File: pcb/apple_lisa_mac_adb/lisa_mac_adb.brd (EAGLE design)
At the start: 56 x 65 mm, 54 parts, among them IC1 STM32F072C8T6, SW1 324_SW, SW2 324_SW, SW3 324_SW

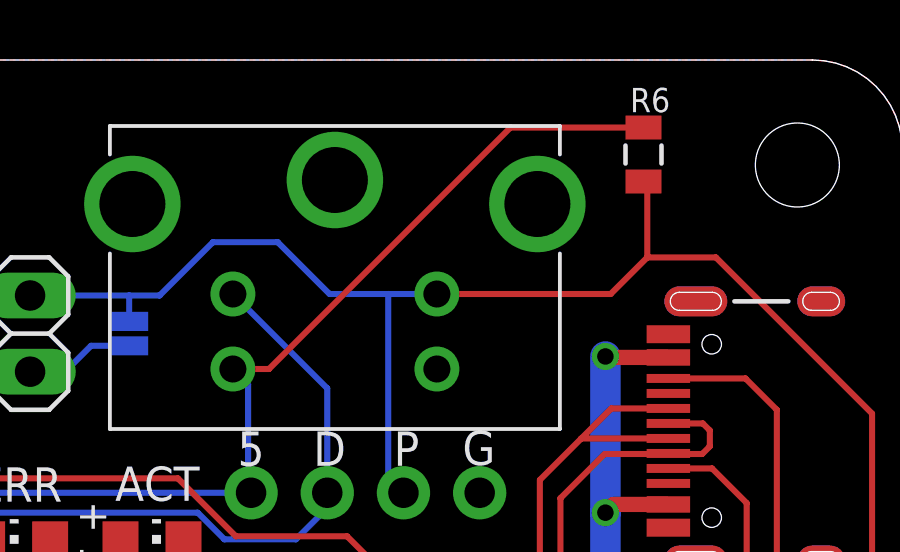
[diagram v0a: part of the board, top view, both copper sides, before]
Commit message: removed ADB power button pullup resistor
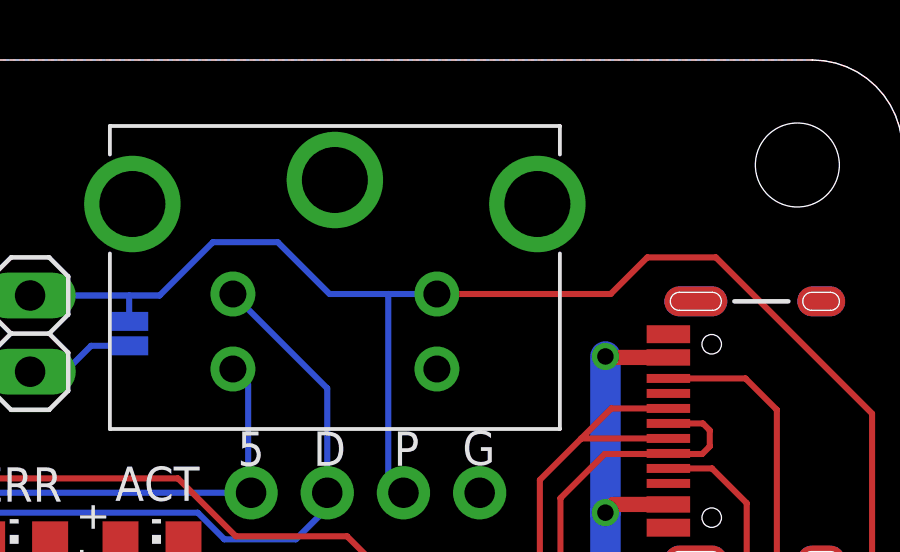
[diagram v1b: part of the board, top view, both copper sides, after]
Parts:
- removed R6: 5.1K, SparkFun-Passives:0805
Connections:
- net N$3: no longer R6.2
- net N$46: no longer R6.1
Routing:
- net N$3: track 49.6 -> 32.6 mm
- net N$46: track 105.1 -> 102.5 mm
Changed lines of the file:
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@@
 <?xml version="1.0" encoding="utf-8"?>
 <!DOCTYPE eagle SYSTEM "eagle.dtd">
-<eagle version="9.6.1">
+<eagle version="9.6.2">
 <drawing>
 <settings>
@@
 <layer number="14" name="Route14" color="22" fill="1" visible="no" active="no"/>
 <layer number="15" name="Route15" color="23" fill="1" visible="no" active="no"/>
-<layer number="16" name="Bottom" color="1" fill="1" visible="no" active="yes"/>
+<layer number="16" name="Bottom" color="1" fill="1" visible="yes" active="yes"/>
 <layer number="17" name="Pads" color="2" fill="1" visible="yes" active="yes"/>
 <layer number="18" name="Vias" color="2" fill="1" visible="yes" active="yes"/>
 <layer number="19" name="Unrouted" color="6" fill="1" visible="yes" active="yes"/>
 <layer number="20" name="Dimension" color="24" fill="1" visible="yes" active="yes"/>
-<layer number="21" name="tPlace" color="7" fill="1" visible="no" active="yes"/>
-<layer number="22" name="bPlace" color="7" fill="1" visible="no" active="yes"/>
+<layer number="21" name="tPlace" color="7" fill="1" visible="yes" active="yes"/>
+<layer number="22" name="bPlace" color="7" fill="1" visible="yes" active="yes"/>
 <layer number="23" name="tOrigins" color="15" fill="1" visible="yes" active="yes"/>
-<layer number="24" name="bOrigins" color="15" fill="1" visible="no" active="yes"/>
-<layer number="25" name="tNames" color="7" fill="1" visible="no" active="yes"/>
-<layer number="26" name="bNames" color="7" fill="1" visible="no" active="yes"/>
-<layer number="27" name="tValues" color="7" fill="1" visible="no" active="yes"/>
-<layer number="28" name="bValues" color="7" fill="1" visible="no" active="yes"/>
+<layer number="24" name="bOrigins" color="15" fill="1" visible="yes" active="yes"/>
+<layer number="25" name="tNames" color="7" fill="1" visible="yes" active="yes"/>
+<layer number="26" name="bNames" color="7" fill="1" visible="yes" active="yes"/>
+<layer number="27" name="tValues" color="7" fill="1" visible="yes" active="yes"/>
+<layer number="28" name="bValues" color="7" fill="1" visible="yes" active="yes"/>
 <layer number="29" name="tStop" color="7" fill="3" visible="no" active="yes"/>
 <layer number="30" name="bStop" color="7" fill="6" visible="no" active="yes"/>
@@
 <layer number="38" name="bTest" color="7" fill="1" visible="no" active="yes"/>
 <layer number="39" name="tKeepout" color="4" fill="11" visible="yes" active="yes"/>
-<layer number="40" name="bKeepout" color="1" fill="11" visible="no" active="yes"/>
+<layer number="40" name="bKeepout" color="1" fill="11" visible="yes" active="yes"/>
 <layer number="41" name="tRestrict" color="4" fill="10" visible="yes" active="yes"/>
-<layer number="42" name="bRestrict" color="1" fill="10" visible="no" active="yes"/>
+<layer number="42" name="bRestrict" color="1" fill="10" visible="yes" active="yes"/>
 <layer number="43" name="vRestrict" color="2" fill="10" visible="no" active="yes"/>
-<layer number="44" name="Drills" color="7" fill="1" visible="no" active="yes"/>
-<layer number="45" name="Holes" color="7" fill="1" visible="no" active="yes"/>
+<layer number="44" name="Drills" color="7" fill="1" visible="yes" active="yes"/>
+<layer number="45" name="Holes" color="7" fill="1" visible="yes" active="yes"/>
 <layer number="46" name="Milling" color="3" fill="1" visible="yes" active="yes"/>
 <layer number="47" name="Measures" color="7" fill="1" visible="no" active="yes"/>
@@
 <layer number="49" name="Reference" color="7" fill="1" visible="no" active="yes"/>
 <layer number="50" name="dxf" color="7" fill="1" visible="no" active="no"/>
-<layer number="51" name="tDocu" color="7" fill="1" visible="no" active="yes"/>
-<layer number="52" name="bDocu" color="7" fill="1" visible="no" active="yes"/>
+<layer number="51" name="tDocu" color="7" fill="1" visible="yes" active="yes"/>
+<layer number="52" name="bDocu" color="7" fill="1" visible="yes" active="yes"/>
 <layer number="53" name="tGND_GNDA" color="7" fill="1" visible="no" active="no"/>
 <layer number="54" name="bGND_GNDA" color="7" fill="1" visible="no" active="no"/>
@@
 <attribute name="VALUE" x="23.749" y="58.42" size="1.27" layer="27" rot="R270"/>
 </element>
-<element name="R6" library="SparkFun-Passives" package="0805" value="5.1K" x="47.371" y="61.849" smashed="yes" rot="R90">
-<attribute name="NAME" x="48.26" y="64.0715" size="0.8128" layer="25" rot="R180"/>
-</element>
 <element name="R17" library="SparkFun-Passives" package="0805" value="100" x="26.797" y="23.749" smashed="yes" rot="R90">
 <attribute name="NAME" x="28.5115" y="22.86" size="0.8128" layer="25" rot="R90"/>
@@
 <wire x1="34.192" y1="54.192" x2="34.192" y2="50.6728" width="0.2032" layer="16"/>
 <wire x1="34.29" y1="50.5748" x2="34.192" y2="50.6728" width="0.2032" layer="16"/>
-<contactref element="R6" pad="2"/>
-<wire x1="47.371" y1="62.749" x2="42.937" y2="62.749" width="0.2032" layer="1"/>
-<wire x1="34.888" y1="54.7" x2="33.684" y2="54.7" width="0.2032" layer="1"/>
-<wire x1="42.937" y1="62.749" x2="34.888" y2="54.7" width="0.2032" layer="1"/>
 <contactref element="R10" pad="2"/>
 <wire x1="13.384" y1="50.606" x2="13.07" y2="50.292" width="0.2032" layer="1"/>
@@
 <wire x1="30.226" y1="57.15" x2="31.242" y2="57.15" width="0.2032" layer="16"/>
 <wire x1="33.02" y1="58.928" x2="31.242" y2="57.15" width="0.2032" layer="16"/>
-<contactref element="R6" pad="1"/>
-<wire x1="47.371" y1="60.949" x2="47.498" y2="60.822" width="0.2032" layer="1"/>
-<wire x1="47.498" y1="60.822" x2="47.498" y2="58.42" width="0.2032" layer="1"/>
 <wire x1="38.862" y1="57.2" x2="38.862" y2="51.0828" width="0.2032" layer="16"/>
 <wire x1="39.37" y1="50.5748" x2="38.862" y2="51.0828" width="0.2032" layer="16"/>
